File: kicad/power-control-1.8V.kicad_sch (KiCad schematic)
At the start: 23 parts, among them J5 USB_C_Receptacle_USB2.0, Q3 DMG2301L, U1 MCP73871, U10 MCP1700x-180xxTT, U11 USBLC6-2P6

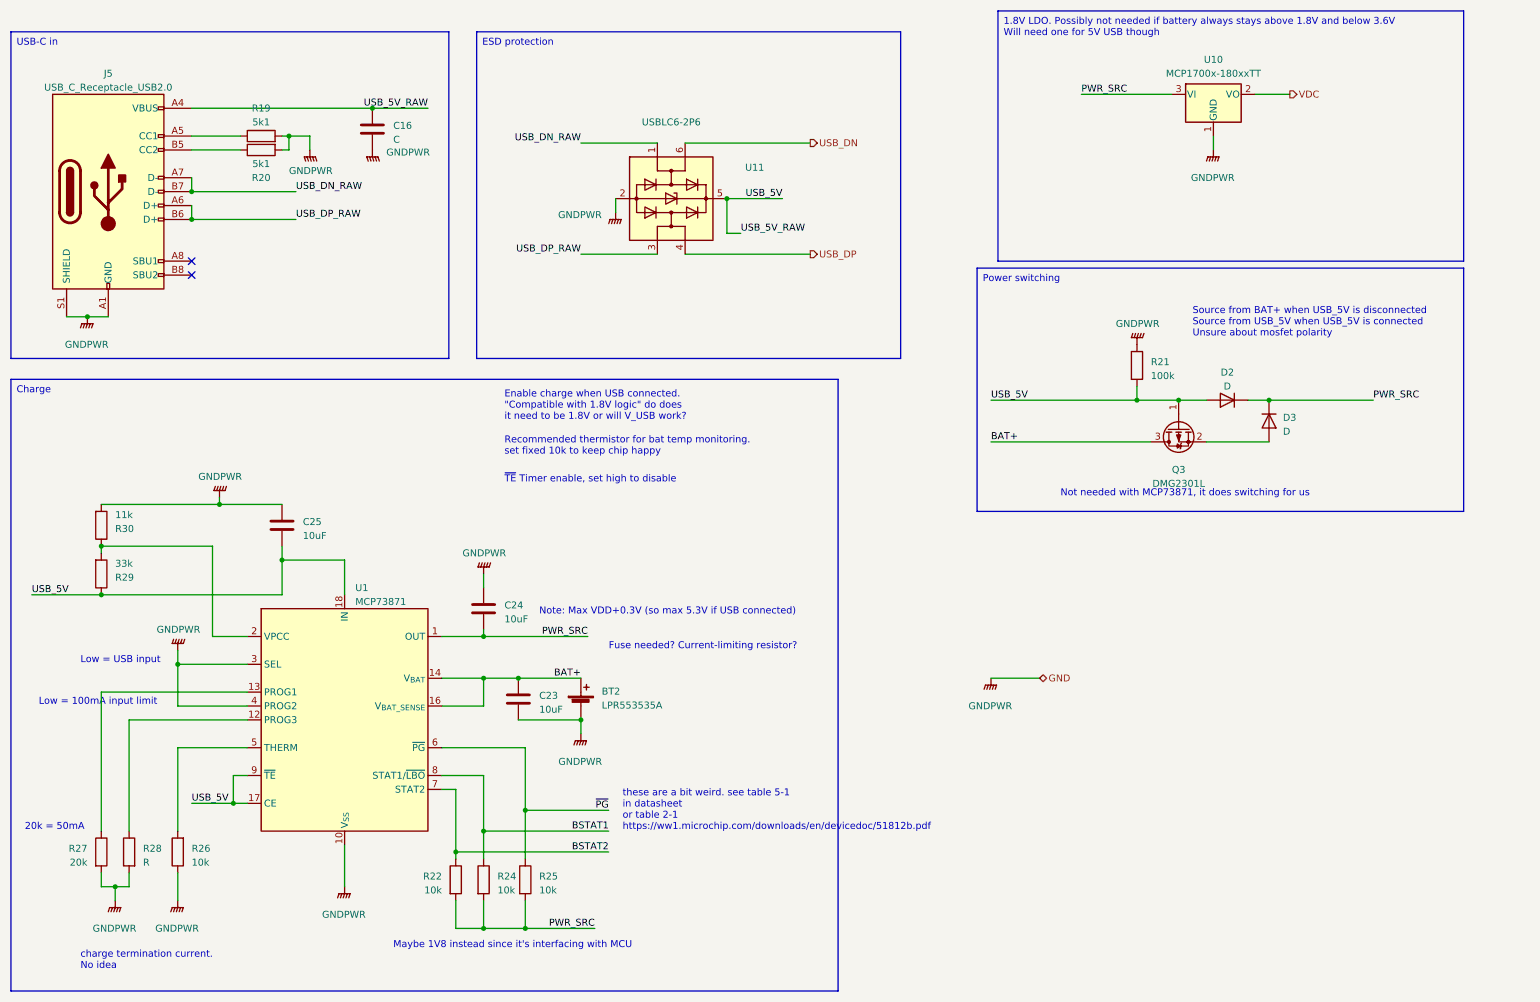
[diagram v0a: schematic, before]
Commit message: Update schematic and add basic PCB layout
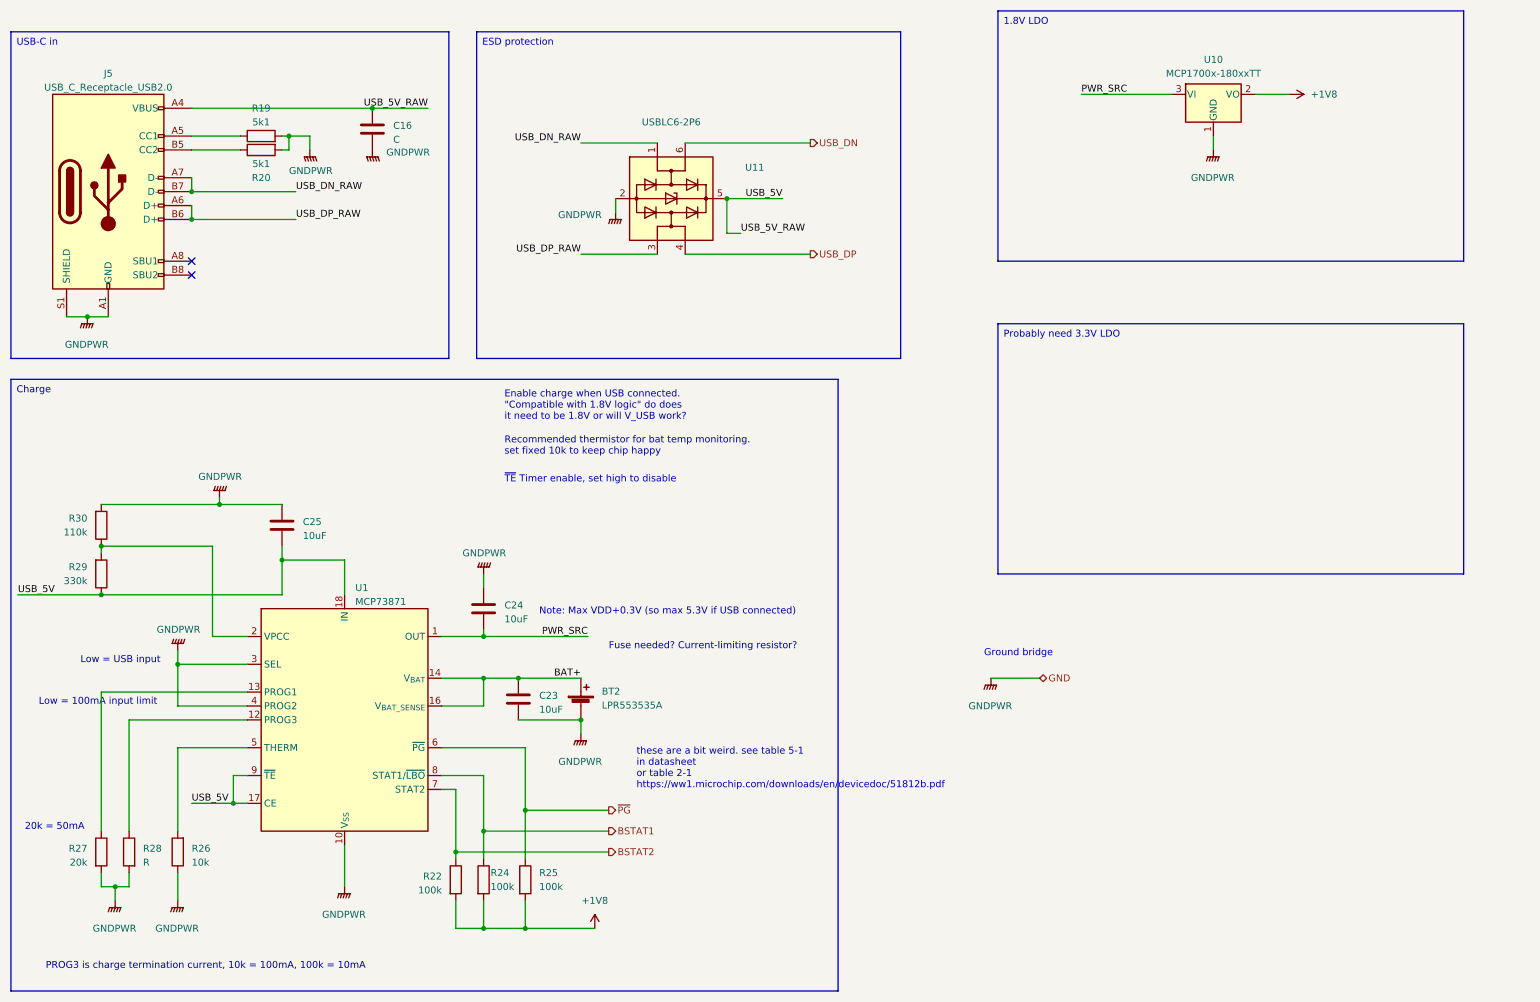
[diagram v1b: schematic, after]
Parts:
- removed D2, D3: D, Diode_SMD:D_0805_2012Metric, symbol Device:D
- removed Q3: DMG2301L, Package_TO_SOT_SMD:SOT-23, symbol Transistor_FET:DMG2301L
- removed R21: 100k, Resistor_SMD:R_0402_1005Metric, symbol Device:R
- BT2: footprint (none) -> Connector_JST:JST_SH_SM02B-SRSS-TB_1x02-1MP_P1.00mm_Horizontal
- C16: footprint (none) -> Capacitor_SMD:C_0603_1608Metric
- C23, C24, C25, R26, R27, R28: footprint (none) -> Capacitor_SMD:C_0402_1005Metric
- R22, R24, R25: value 10k -> 100k; footprint (none) -> Capacitor_SMD:C_0402_1005Metric
- R29: value 33k -> 330k; footprint (none) -> Capacitor_SMD:C_0402_1005Metric
- R30: value 11k -> 110k; footprint (none) -> Capacitor_SMD:C_0402_1005Metric
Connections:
- net PWR_SRC: no longer R22.2, R24.2, R25.2
- net VDC renamed +1V8
- net +1V8: now also R22.2, R24.2, R25.2
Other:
- note added: "Ground bridge"
- note added: "PROG3 is charge termination current, 10k = 100mA, 100k = 10mA"
- note removed: "Maybe 1V8 instead since it's interfacing with MCU"
- note removed: "Not needed with MCP73871, it does switching for us"
- note removed: "Source from BAT+ when USB_5V is disconnected Source from USB_5V when USB_5V is connected Unsure about mosfet polarity"
- note removed: "charge termination current. No idea"

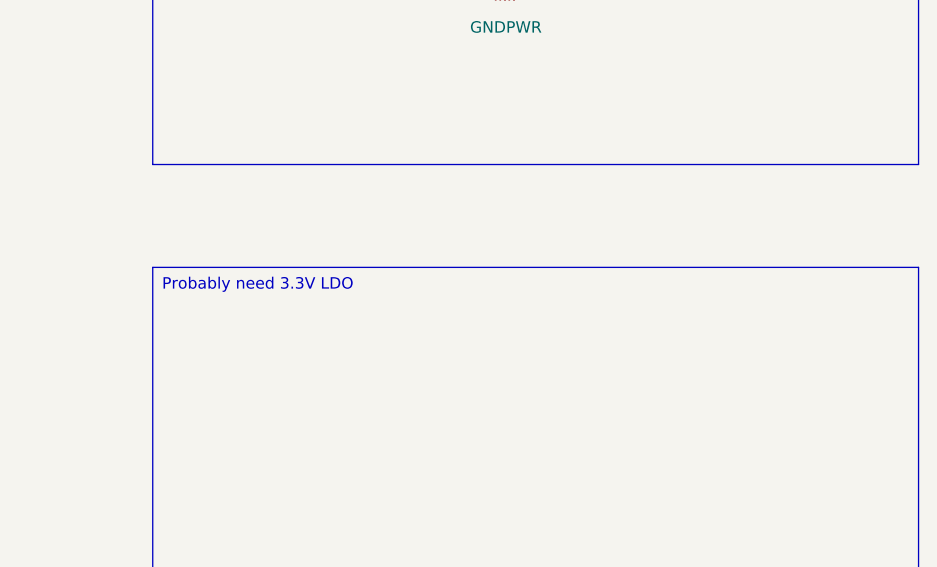
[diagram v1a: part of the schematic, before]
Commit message: comments about power, changed eeprom and flash packages
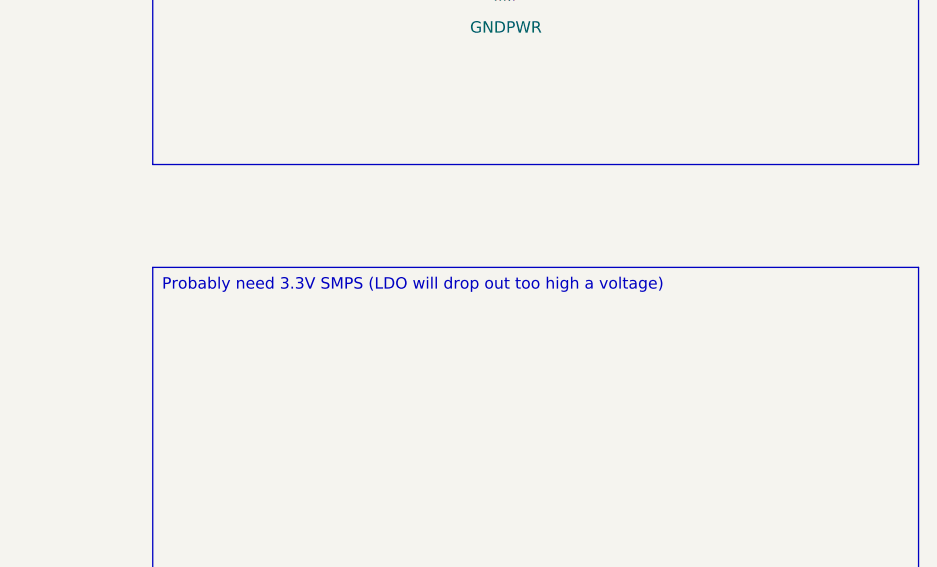
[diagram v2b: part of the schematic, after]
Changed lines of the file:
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@@
     (effects (font (size 1.27 1.27)) (justify left top))
   )
-  (text_box "Probably need 3.3V LDO"
+  (text_box "Probably need 3.3V SMPS (LDO will drop out too high a voltage)"
     (at 198.12 71.12 0) (size 85.09 45.72)
     (stroke (width 0) (type default))

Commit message: playing with battery/power circuit
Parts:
- removed R29: 330k, Capacitor_SMD:C_0402_1005Metric, symbol Device:R
- removed R30: 110k, Capacitor_SMD:C_0402_1005Metric, symbol Device:R
- BT1: renamed from BT2; value LPR553535A -> HZ553535
- R27: value 20k -> 8k3
- R28: value R -> 100k
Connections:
- net GNDPWR: now also C25.2, U1.9 (~{TE}); no longer C25.1, U1.4 (PROG2)
- net USB_5V: now also C25.1, U1.2 (VPCC), U1.4 (PROG2); no longer C25.2, U1.9 (~{TE})
- net BAT+: no longer names the net of BT1.1 (+), C23.1, U1.14 (V_{BAT}), U1.15 (V_{BAT}), U1.16 (V_{BAT_SENSE})
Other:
- note added: "(1)"
- note added: "(1) 8k3 = 120mA max charge"
- note added: "(2)"
- note added: "(2) High = 500mA input limit"
- note added: "(3)"
- note added: "(3) 100k = 10mA charge current cutoff"
- note added: "(4)"
- note added: "(4) 10k resistor to disable temperature sense"
- note added: "(5)"
- note added: "(5) Always enable charge timer control"
- note added: "(6)"
- note added: "(6) Only enable charge on USB power. Needs pull-down?"
- note added: "(7)"
- note added: "(7) Switches between battery and USB power. Max 5.3V"
- note added: "Good place to measure system current draw"
- note added: "Max charge voltage 4.2V 0.2C (120mA) const current down to limit of 0.01C (6mA)"
- note added: "Watch for thermals when in a case"
- note added: "Watch for thermals when in a case and on charge"
- note removed: "20k = 50mA"
- note removed: "Enable charge when USB connected. "Compatible with 1.8V logic" do does it need to be 1.8V or will V_USB work?"
- note removed: "Fuse needed? Current-limiting resistor?"
- note removed: "Low = 100mA input limit"
- note removed: "Note: Max VDD+0.3V (so max 5.3V if USB connected)"
- note removed: "PROG3 is charge termination current, 10k = 100mA, 100k = 10mA"
- note removed: "Recommended thermistor for bat temp monitoring. set fixed 10k to keep chip happy"
- note removed: "~{TE} Timer enable, set high to disable"
- moved on the sheet: C25
